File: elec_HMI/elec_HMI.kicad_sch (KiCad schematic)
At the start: 22 parts, among them J1 JST SH, J2 JST SH, U1 BMI088

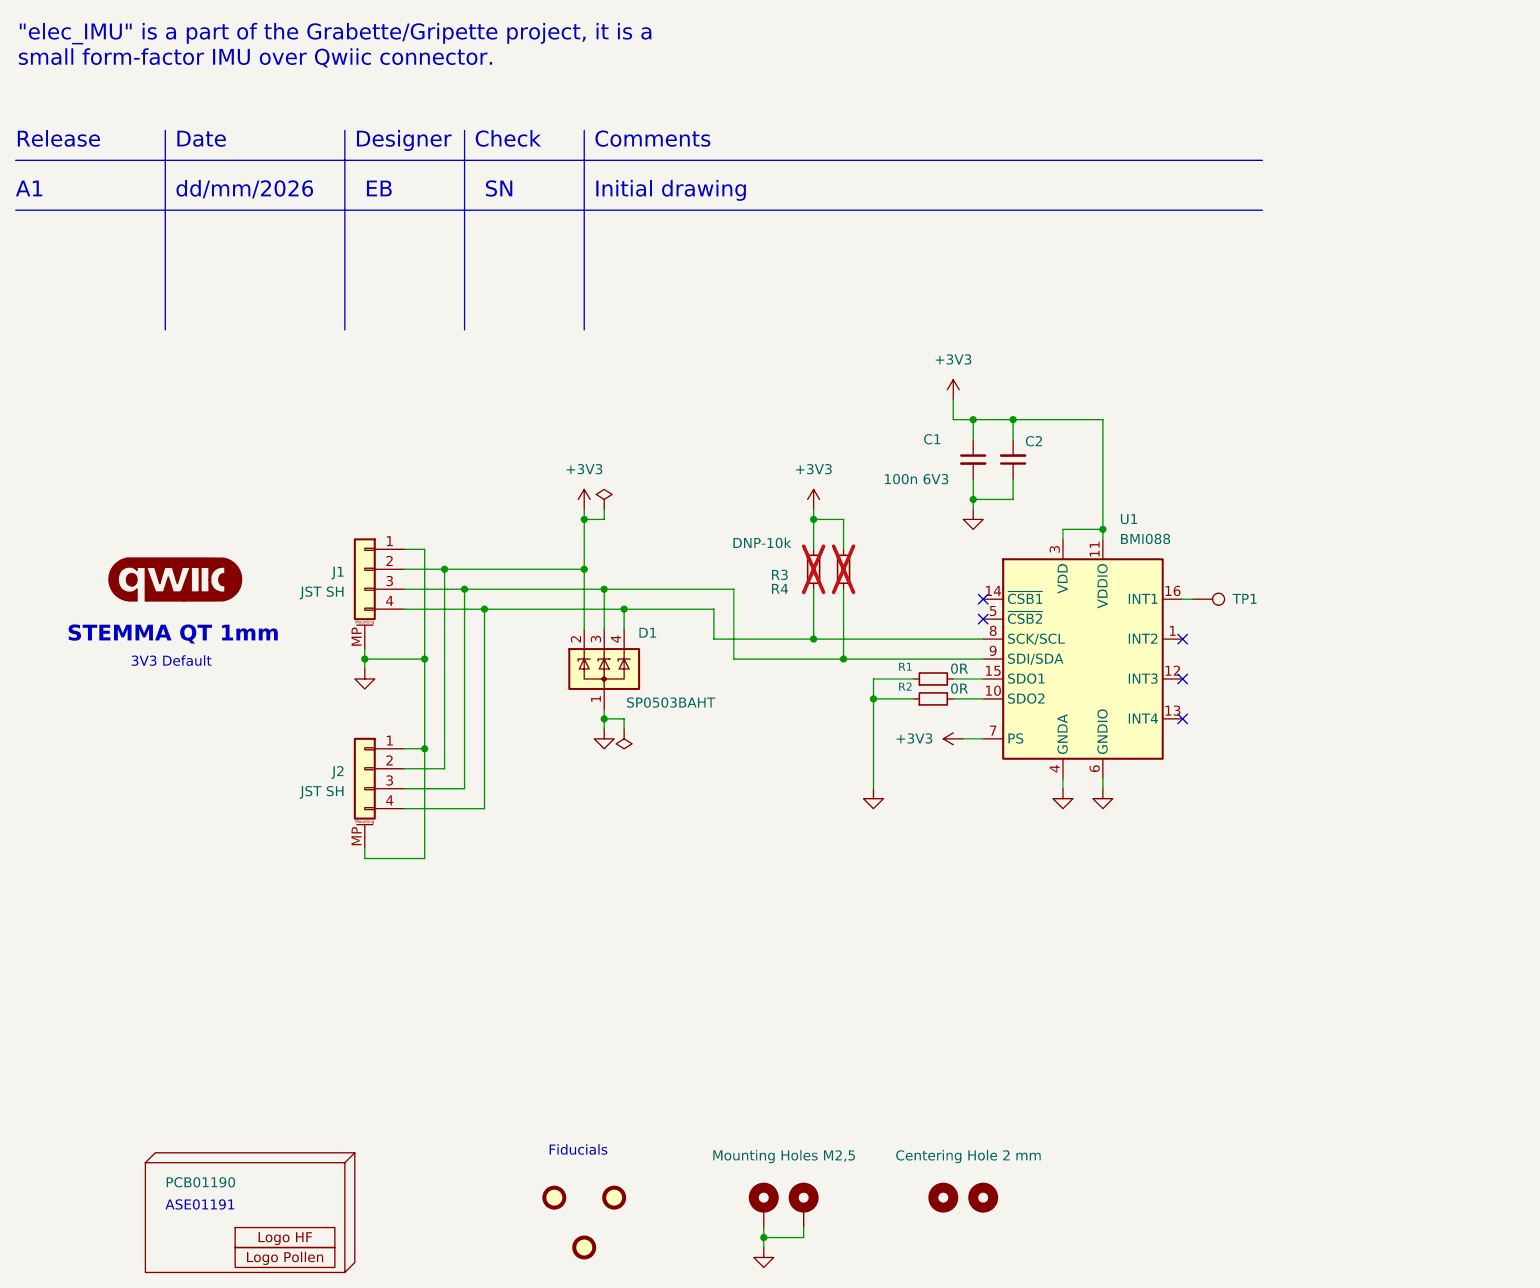
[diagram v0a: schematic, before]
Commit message: [update] Angle+IMU are routed ERC OK
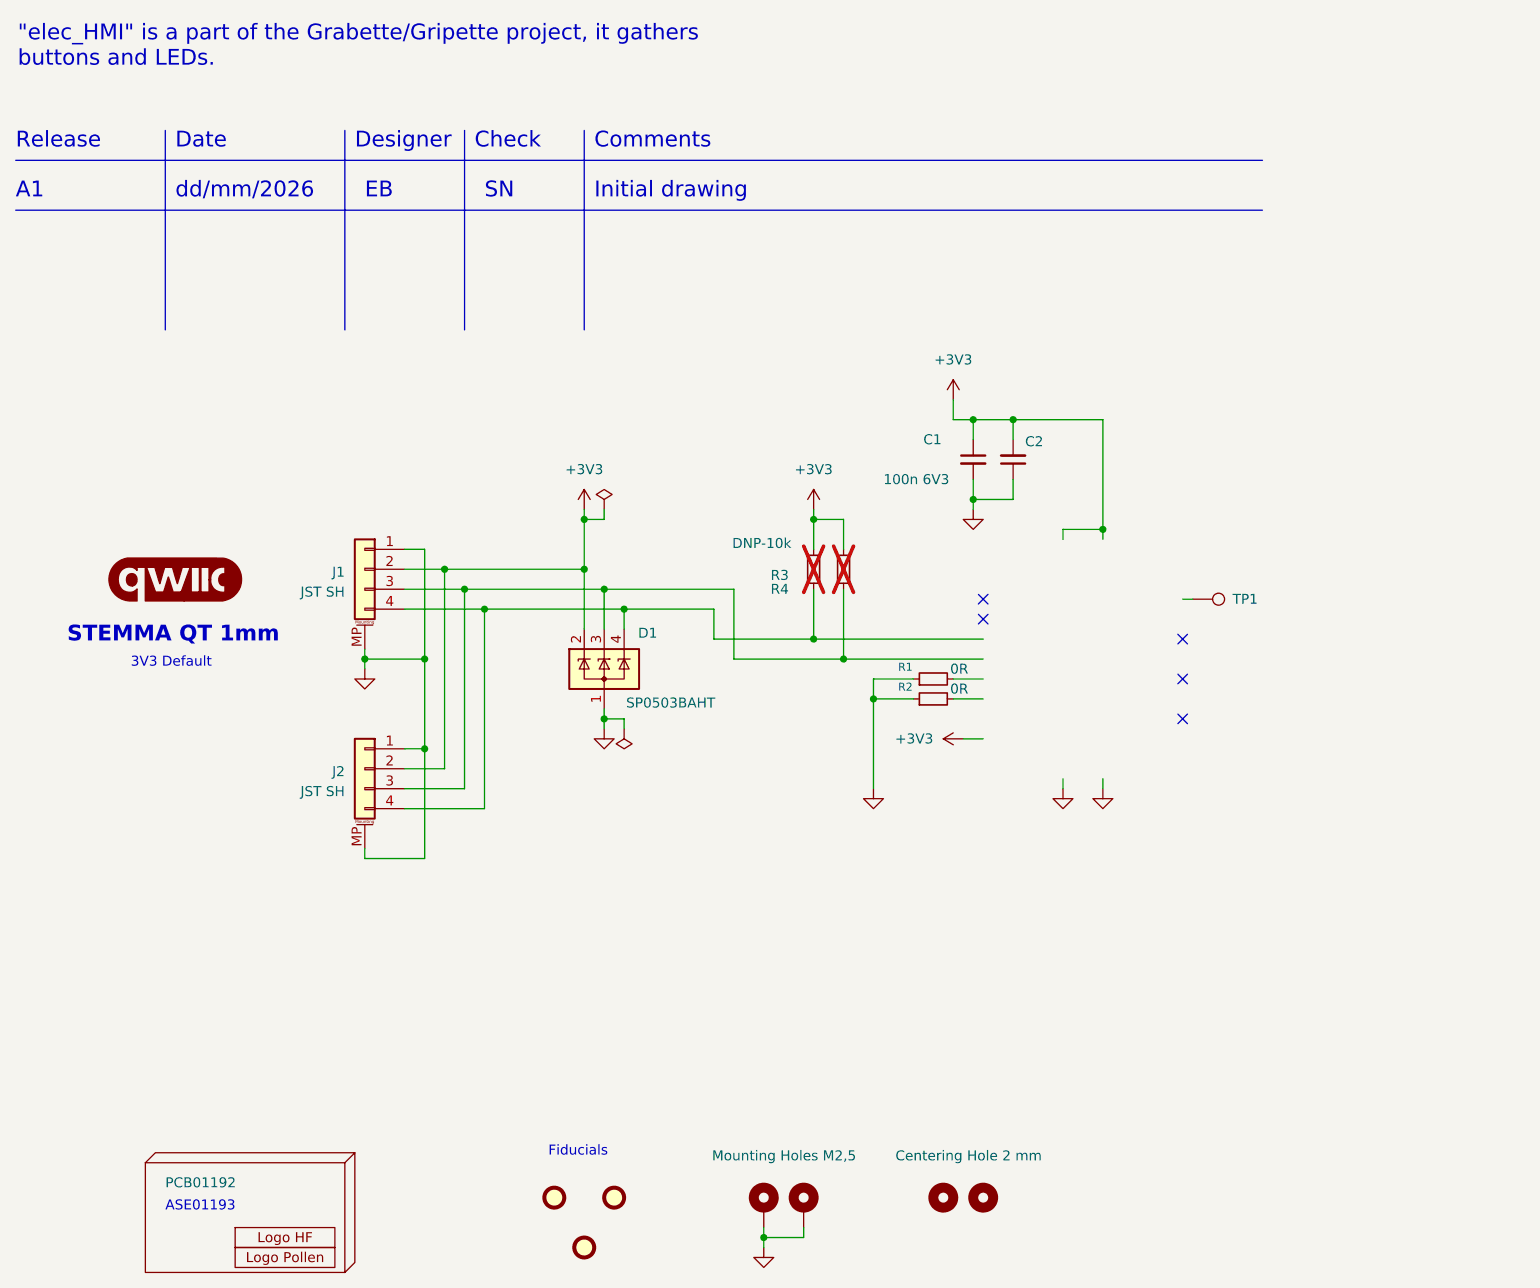
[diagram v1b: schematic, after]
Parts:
- removed U1: BMI088, Package_LGA:Bosch_LGA-16_4.5x3mm_P0.5mm_LayoutBorder7x1y_ClockwisePinNumbering, symbol Sensor_Motion:BMI088
- H1: value PCB01190 -> PCB01192
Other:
- note added: ""elec_HMI" is a part of the Grabette/Gripette project, it gathers buttons and LEDs."
- note added: "ASE01193"
- note removed: ""elec_IMU" is a part of the Grabette/Gripette project, it is a small form-factor IMU over Qwiic connector."
- note removed: "ASE01191"
- title: Grabette - IMU -> Grabette - HMI
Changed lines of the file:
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@@
 	(paper "A4")
 	(title_block
-		(title "Grabette - IMU")
-		(date "2026-03-12")
+		(title "Grabette - HMI")
+		(date "2026-03-17")
 		(rev "A1")
 		(company "Pollen Robotics/HF")
@@
 		)
 	)
-	(text "ASE01191"
+	(text "ASE01193"
 		(exclude_from_sim no)
 		(at 38.1 173.355 0)
@@
 		)
 	)
-	(text "\"elec_IMU\" is a part of the Grabette/Gripette project, it is a \nsmall form-factor IMU over Qwiic connector."
+	(text "\"elec_HMI\" is a part of the Grabette/Gripette project, it gathers \nbuttons and LEDs."
 		(exclude_from_sim no)
 		(at 19.304 27.686 0)
@@
 			)
 		)
-		(property "Value" "PCB01190"
+		(property "Value" "PCB01192"
 			(at 38.1 169.545 0)
 			(effects
@@
 					(unit 1)
 				)
-			)
-		)
-	)
-	(symbol
-		(lib_id "Sensor_Motion:BMI088")
-		(at 154.94 102.87 0)
-		(unit 1)
-		(exclude_from_sim no)
-		(in_bom yes)
-		(on_board yes)
-		(dnp no)
-		(fields_autoplaced yes)
-		(property "Reference" "U1"
-			(at 159.6233 85.09 0)
-			(effects
-				(font
-					(size 1.27 1.27)
-				)
-				(justify left)
-			)
-		)
-		(property "Value" "BMI088"
-			(at 159.6233 87.63 0)
-			(effects
-				(font
-					(size 1.27 1.27)
-				)
-				(justify left)
-			)
-		)
-		(property "Footprint" "Package_LGA:Bosch_LGA-16_4.5x3mm_P0.5mm_LayoutBorder7x1y_ClockwisePinNumbering"
-			(at 138.43 104.14 0)
-			(effects
-				(font
-					(size 1.27 1.27)
-				)
-				(hide yes)
-			)
-		)
-		(property "Datasheet" "https://www.bosch-sensortec.com/media/boschsensortec/downloads/datasheets/bst-bmi088-ds001.pdf"
-			(at 138.43 104.14 0)
-			(effects
-				(font
-					(size 1.27 1.27)
-				)
-				(hide yes)
-			)
-		)
-		(property "Description" "Inertial Measurement Unit"
-			(at 154.94 102.87 0)
-			(effects
-				(font
-					(size 1.27 1.27)
-				)
-				(hide yes)
-			)
-		)
-		(property "FT Rotation Offset" "180"
-			(at 154.94 102.87 0)
-			(effects
-				(font
-					(size 1.27 1.27)
-				)
-				(hide yes)
-			)
-		)
-		(property "LCSC Part" "C194919"
-			(at 154.94 102.87 0)
-			(effects
-				(font
-					(size 1.27 1.27)
-				)
-				(hide yes)
-			)
-		)
-		(property "Man." "Bosch Sensortec"
-			(at 154.94 102.87 0)
-			(effects
-				(font
-					(size 1.27 1.27)
-				)
-				(hide yes)
-			)
-		)
-		(property "Man. Ref." "BMI088"
-			(at 154.94 102.87 0)
-			(effects
-				(font
-					(size 1.27 1.27)
-				)
-				(hide yes)
-			)
-		)
-		(pin "6"
-		)
-		(pin "2"
-		)
-		(pin "4"
-		)
-		(pin "1"
-		)
-		(pin "7"
-		)
-		(pin "15"
-		)
-		(pin "13"
-		)
-		(pin "12"
-		)
-		(pin "16"
-		)
-		(pin "11"
-		)
-		(pin "10"
-		)
-		(pin "3"
-		)
-		(pin "5"
-		)
-		(pin "9"
-		)
-		(pin "14"
-		)
-		(pin "8"
-		)
-		(instances
-			(project "elec_IMU"
-				(path "/bc05f5da-608c-4912-90e4-36b13d989976"
-					(reference "U1")
-					(unit 1)
-				)

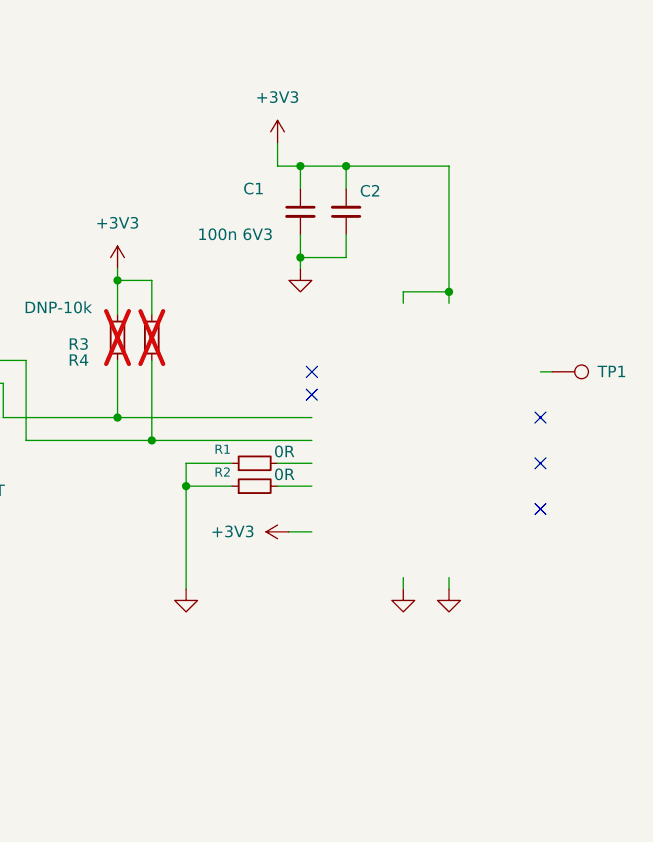
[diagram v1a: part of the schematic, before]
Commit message: [update] IMU + angle sensor RC1
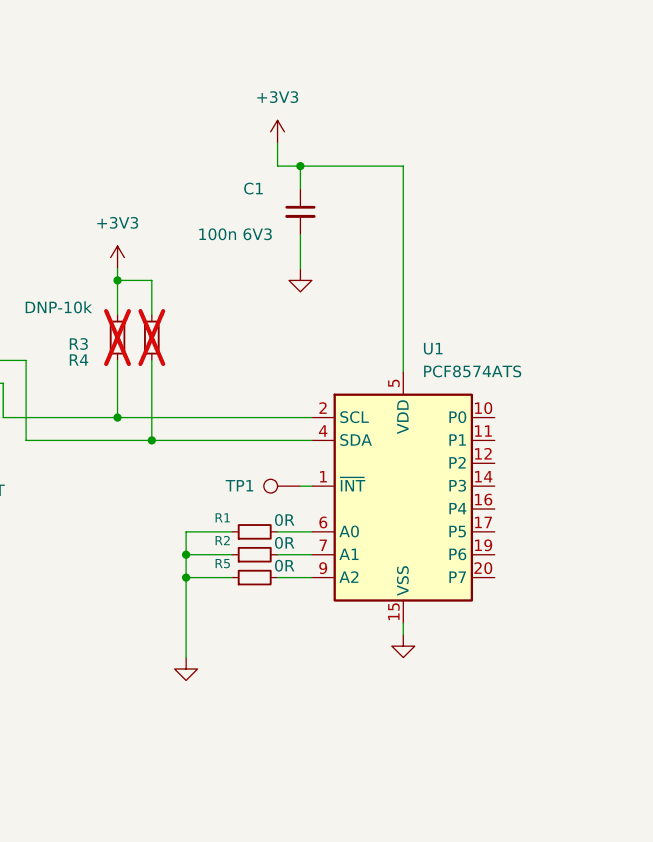
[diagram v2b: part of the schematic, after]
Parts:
- removed C2: 100n 6V3, Capacitor_SMD:C_0402_1005Metric, symbol Device:C_Small
- added R5: 0R, Resistor_SMD:R_0402_1005Metric, symbol Device:R_Small
- added U1: PCF8574ATS, Package_SO:SSOP-20_4.4x6.5mm_P0.65mm, symbol Interface_Expansion:PCF8574ATS
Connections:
- net +3V3: now also U1.5 (VDD)
- net GND: now also R5.1, U1.15 (VSS)
- net at D1.4 (K), J1.4 (Pin_4), J2.4 (Pin_4)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: now also U1.2 (SCL)
- net at D1.3 (K), J1.3 (Pin_3), J2.3 (Pin_3)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: now also U1.4 (SDA)
- net at R2.2: now also U1.7 (A1)
- net at TP1.1: now also U1.1 (~{INT})
- net at R1.2: now also U1.6 (A0)
- new net: R5.2, U1.9 (A2)
- no-connect marks 5 -> 0
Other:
- moved on the sheet: R1, R2, TP1

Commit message: [added] Wiring Diagrams
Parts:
- added D2: Green, LED_SMD:LED_0603_1608Metric, symbol Device:LED_Small
- added D3: Red, LED_SMD:LED_0603_1608Metric, symbol Device:LED_Small
- added D4: Blue, LED_SMD:LED_0603_1608Metric, symbol Device:LED_Small
- added R10, R8, R9: 470R, Resistor_SMD:R_0402_1005Metric, symbol Device:R_Small
- added R6, R7: 10k, Resistor_SMD:R_0402_1005Metric, symbol Device:R_Small
- added SW1, SW2: SW_SPST, Button_Switch_Keyboard:SW_Cherry_MX_1.00u_PCB, symbol Switch:SW_SPST
- added TP2: TestPoint, TestPoint:TestPoint_Loop_D2.50mm_Drill1.0mm_LowProfile, symbol Connector:TestPoint
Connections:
- net +3V3: now also R6.1, R7.1
- net GND: now also D2.1 (K), D3.1 (K), D4.1 (K), SW1.2 (B), SW2.2 (B)
- net at U1.10 (P0): now also R6.2, SW1.1 (A)
- net at U1.11 (P1): now also R7.2, SW2.1 (A)
- net at U1.12 (P2): now also TP2.1
- net at U1.16 (P4): now also R9.2
- net at U1.17 (P5): now also R8.2
- net at U1.19 (P6): now also R10.2
- new net: D3.2 (A), R9.1
- new net: D2.2 (A), R8.1
- new net: D4.2 (A), R10.1
- no-connect marks 0 -> 2
